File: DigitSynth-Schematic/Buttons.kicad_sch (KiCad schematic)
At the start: 0 parts

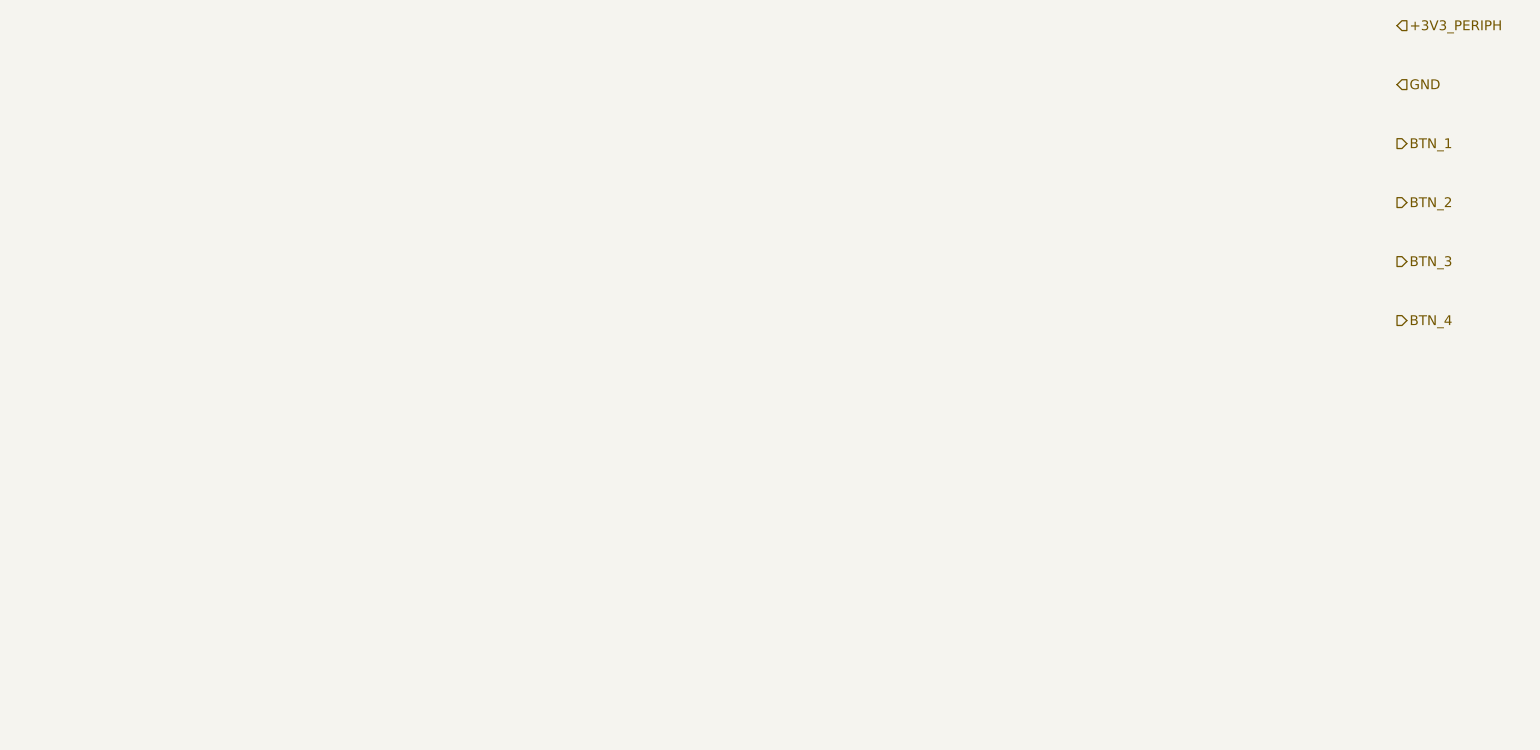
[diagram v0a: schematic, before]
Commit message: Add completed KiCad schematic hierarchy (Pi interface, ADC, LEDs, buttons, power)
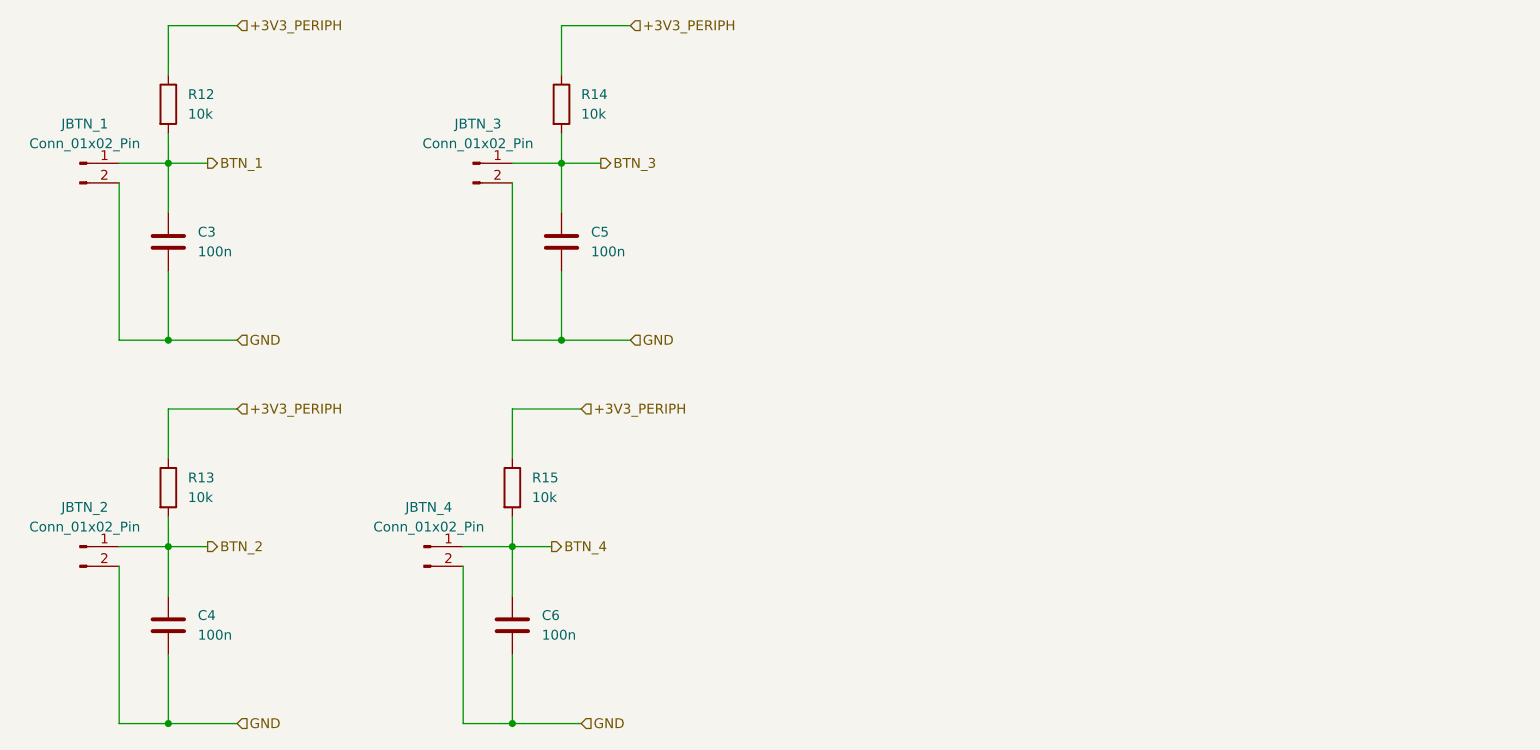
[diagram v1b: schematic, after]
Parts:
- added C3, C4, C5, C6: 100n, symbol Device:C
- added JBTN_1, JBTN_2, JBTN_3, JBTN_4: Conn_01x02_Pin, symbol Connector:Conn_01x02_Pin
- added R12, R13, R14, R15: 10k, symbol Device:R
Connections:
- net +3V3_PERIPH: now also R12.1, R13.1, R14.1, R15.1
- net BTN_1: now also C3.1, JBTN_1.1 (BTN), R12.2
- net BTN_2: now also C4.1, JBTN_2.1 (BTN), R13.2
- net BTN_3: now also C5.1, JBTN_3.1 (BTN), R14.2
- net BTN_4: now also C6.1, JBTN_4.1 (BTN), R15.2
- net GND: now also C3.2, C4.2, C5.2, C6.2, JBTN_1.2 (GND), JBTN_2.2 (GND), JBTN_3.2 (GND), JBTN_4.2 (GND)
